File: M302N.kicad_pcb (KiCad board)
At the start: 2 copper layers, 100.1 x 56 mm, 31 parts, among them J1 DC12V, J10 ADC_IN, J11 RJ45, J12 DC12V FAN, J13 Conn_01x05_Socket, J14 Conn_01x05_Socket, J18 Conn_01x04_Socket, J19 Conn_01x04_Socket, J2 UART, J3 extend I/O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

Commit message: PCBほぼ完成
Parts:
- added REF**: MountingHole_2.7mm_M2.5_Pad, MountingHole:MountingHole_2.7mm_M2.5_Pad, F.Cu at (167.0, 109.9)
- added REF**: MountingHole_2.7mm_M2.5_Pad, MountingHole:MountingHole_2.7mm_M2.5_Pad, F.Cu at (81.3, 62.9)
- added REF**: MountingHole_2.7mm_M2.5_Pad, MountingHole:MountingHole_2.7mm_M2.5_Pad, F.Cu at (167.0, 62.9)
- added REF**: MountingHole_2.7mm_M2.5_Pad, MountingHole:MountingHole_2.7mm_M2.5_Pad, F.Cu at (75.6, 109.9)
- moved R1 5.20 mm to (80.6, 105.4), turned to 90 degrees
- moved C6 2.03 mm to (88.1, 64.8), turned to 0 degrees
- moved J19 0.27 mm to (132.8, 79.9)
- turned C4 to 90 degrees
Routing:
- net Net-(D2-K): track 8.78 -> 6.16 mm
- net +5V: track 160.8 -> 162.0 mm
- net /*D3: track 77.6 -> 76.8 mm
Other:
- board text added: "+"
- board text added: "+12V"
- board text added: "+5V"
- board text added: "A"
- board text added: "A0"
- board text added: "A1"
- board text added: "A2"
- board text added: "D4"
- board text added: "D5"
- board text added: "D6"
- board text added: "D7"
- board text added: "D8"
- board text added: "D9"
- board text added: "GND"
- board text added: "K"
- board text added: "M302N Ver. 1.00 2025 Mar."
- board text added: "RX"
- board text added: "SIG"
- board text added: "TX"
- board text added: "UECS観測ノード"
- board text added: "YS Lab"

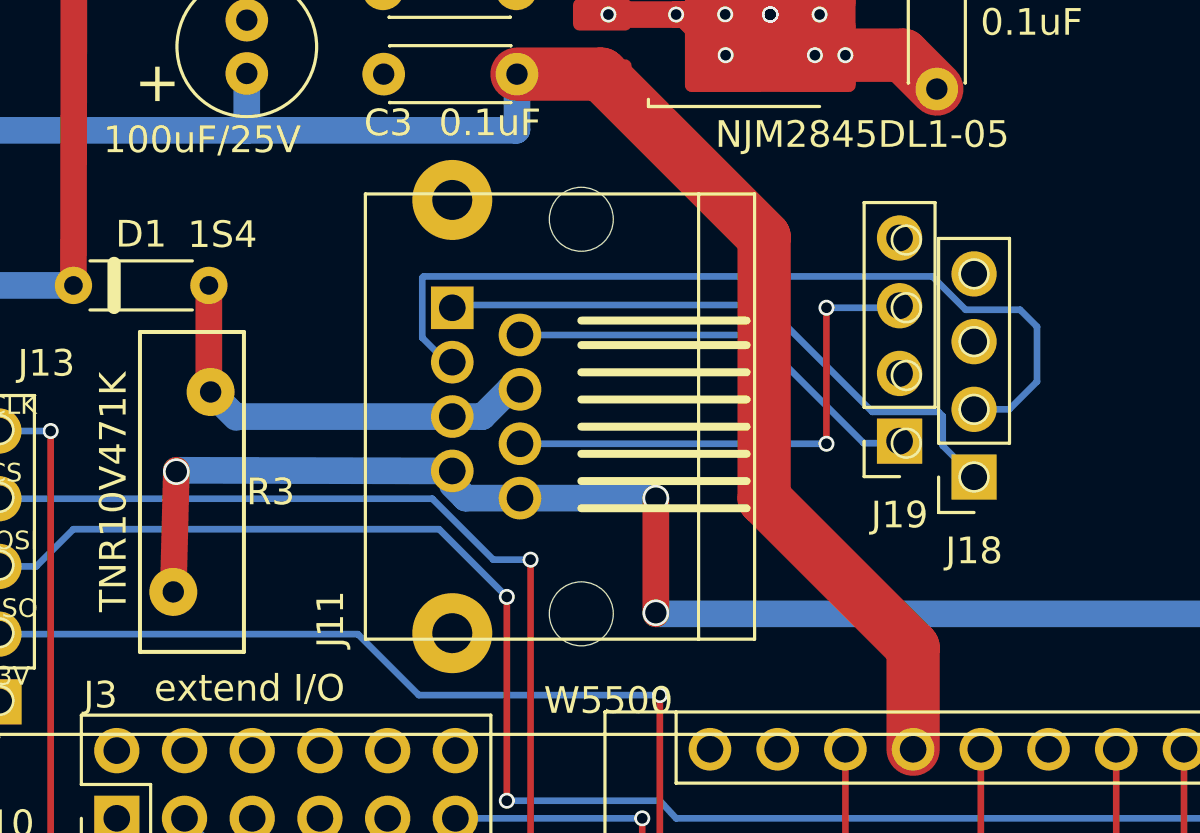
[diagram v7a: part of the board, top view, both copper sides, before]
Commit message: 3Dデータ更新とRJ45コネクタの取り付け位置微妙に変更
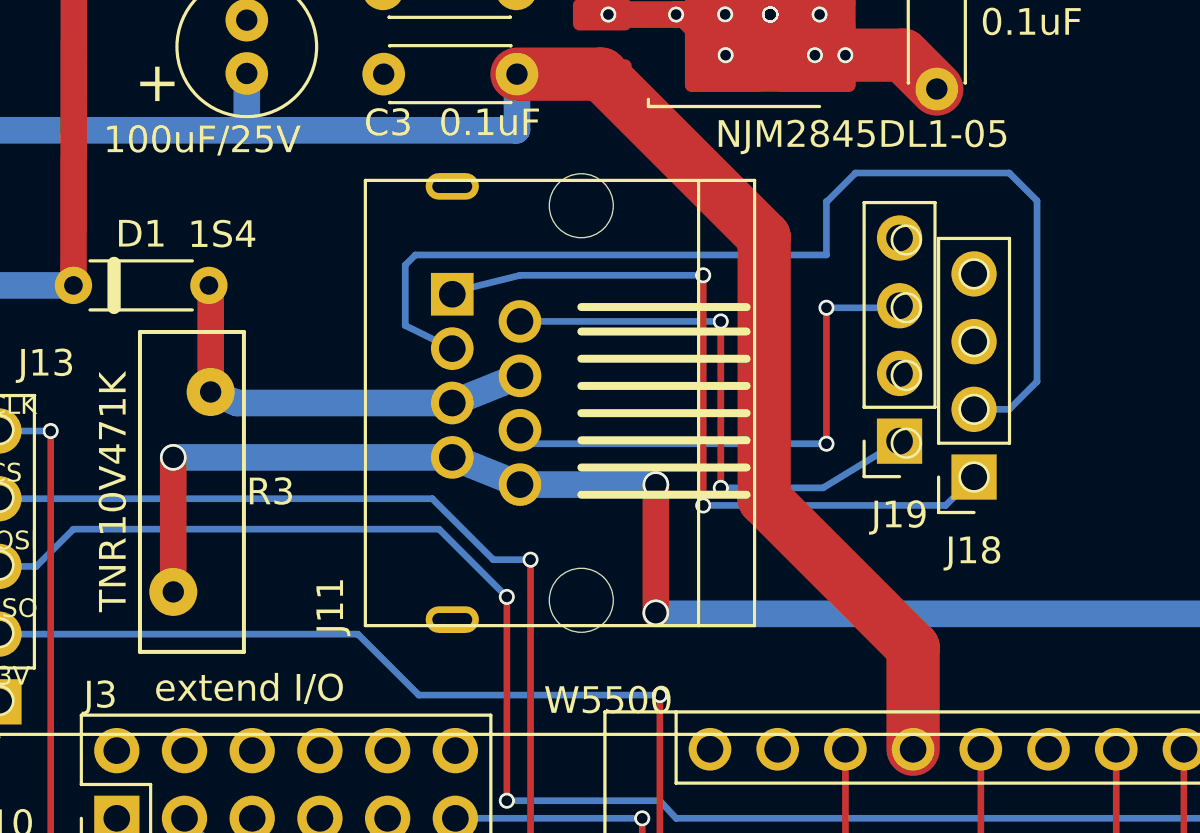
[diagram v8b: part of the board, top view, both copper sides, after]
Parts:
- moved J11 0.51 mm to (120.9, 78.5)
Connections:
- J11 pad : (no net) -> GND
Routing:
- net Net-(J18-Pin_2): track 32.5 -> 40.5 mm
- net Net-(J18-Pin_1): track 22.9 -> 28.8 mm, vias 0 -> 2
- net Net-(J19-Pin_1): track 16.2 -> 21.0 mm, vias 0 -> 2
- net Net-(J1-Pad2): track 75.5 -> 76.1 mm
- net Net-(D1-A): track 16.4 -> 15.9 mm
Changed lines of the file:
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@@
 	(footprint "HOLLY2:RJ45_Neltron_7810-8P8C"
 		(layer "F.Cu")
-		(at 120.904 78.96 90)
+		(at 120.904 78.452 90)
 		(descr "RJ45 Socket 秋月通商 http://akizukidenshi.com/catalog/g/gC-00159/")
 		(property "Reference" "J11"
@@
 			(layer "F.CrtYd")
 		)
-		(pad "" thru_hole circle
+		(pad "" thru_hole oval
 			(at -8.125 -4.84 90)
-			(size 3 3)
-			(drill 1.5)
+			(size 1 2)
+			(drill oval 0.5 1.5)
 			(layers "*.Cu" "*.Mask" "In1.Cu" "In2.Cu" "In3.Cu" "In4.Cu" "In5.Cu" "In6.Cu"
 				"In7.Cu" "In8.Cu" "In9.Cu" "In10.Cu" "In11.Cu" "In12.Cu" "In13.Cu" "In14.Cu"
@@
 			)
 			(remove_unused_layers no)
+			(net 13 "GND")
 		)
 		(pad "" np_thru_hole circle
@@
 			)
 		)
-		(pad "" thru_hole circle
+		(pad "" thru_hole oval
 			(at 8.125 -4.84 90)
-			(size 3 3)
-			(drill 1.5)
+			(size 1 2)
+			(drill oval 0.5 1.5)
 			(layers "*.Cu" "*.Mask" "In1.Cu" "In2.Cu" "In3.Cu" "In4.Cu" "In5.Cu" "In6.Cu"
 				"In7.Cu" "In8.Cu" "In9.Cu" "In10.Cu" "In11.Cu" "In12.Cu" "In13.Cu" "In14.Cu"
@@
 			)
 			(remove_unused_layers no)
+			(net 13 "GND")
 		)
 		(pad "1" thru_hole rect
@@
 		)
 		(pad "2" thru_hole circle
-			(at 7.5 1.4 90)
+			(at 7.5 1.401 90)
 			(size 1.8 1.8)
 			(drill 0.8)
@@
 		(tags "C Disc series Radial pin pitch 5.00mm  diameter 4.3mm width 1.9mm Capacitor")
 		(property "Reference" "C6"
-			(at 0.04 -2.159 360)
+			(at 0.04 -2.159 0)
 			(layer "F.SilkS")
 			(effects
@@
 	)
 	(segment
-		(start 106.934 74.041)
-		(end 106.934 77.973)
+		(start 107 74.041)
+		(end 107 77.973)
 		(width 1)
 		(layer "F.Cu")
@@
 	)
 	(segment
-		(start 116.064 78.96)
-		(end 117.19537 78.96)
-		(width 1)
-		(layer "B.Cu")
-		(net 25)
-	)
-	(segment
 		(start 106.934 77.973)
 		(end 106.999 78.038)
@@
 	)
 	(segment
-		(start 117.19537 78.96)
-		(end 118.21537 77.94)
+		(start 116.064 78.452)
+		(end 118.604 77.432)
 		(width 1)
 		(layer "B.Cu")
@@
 	(segment
 		(start 106.999 78.038)
-		(end 107.955 78.994)
-		(width 1)
-		(layer "B.Cu")
-		(net 25)
-	)
-	(segment
-		(start 107.989 78.96)
-		(end 116.064 78.96)
+		(end 107.989 78.452)
 		(width 1)
 		(layer "B.Cu")
@@
 	)
 	(segment
-		(start 118.21537 77.94)
-		(end 118.604 77.94)
+		(start 107.989 78.452)
+		(end 116.064 78.452)
 		(width 1)
 		(layer "B.Cu")
@@
 	)
 	(segment
-		(start 123.7 82.02)
+		(start 123.7 81.512)
 		(end 123.7 86.36)
 		(width 1)
@@
 	)
 	(segment
-		(start 105.7148 80.9752)
-		(end 105.713511 81.026)
-		(width 1)
-		(layer "F.Cu")
-		(net 27)
-	)
-	(segment
-		(start 105.713511 81.026)
+		(start 105.599 80.492)
 		(end 105.599 85.538)
 		(width 1)
@@
 	)
 	(via
-		(at 123.7 82.02)
+		(at 123.7 81.512)
 		(size 1)
 		(drill 0.8)
@@
 	)
 	(via
-		(at 105.713511 81.026)
+		(at 105.599 80.492)
 		(size 1)
 		(drill 0.8)
@@
 	)
 	(segment
-		(start 116.064 81)
-		(end 116.064 81.52)
-		(width 0.25)
-		(layer "B.Cu")
-		(net 27)
-	)
-	(segment
-		(start 116.064 81)
-		(end 105.7148 80.9752)
-		(width 1)
-		(layer "B.Cu")
-		(net 27)
-	)
-	(segment
-		(start 118.604 82.02)
-		(end 123.7 82.02)
+		(start 116.064 80.492)
+		(end 105.599 80.492)
 		(width 1)
 		(layer "B.Cu")
@@
 	)
 	(segment
-		(start 116.064 81.52)
-		(end 116.564 82.02)
+		(start 118.604 81.512)
+		(end 123.7 81.512)
 		(width 1)
 		(layer "B.Cu")
@@
 	)
 	(segment
-		(start 116.564 82.02)
-		(end 118.604 82.02)
+		(start 116.064 80.492)
+		(end 118.604 81.512)
 		(width 1)
 		(layer "B.Cu")
@@
 	)
 	(segment
-		(start 118.604 75.9)
-		(end 127.4366 75.9)
+		(start 126.136 75.392)
+		(end 126.136 81.636)
 		(width 0.25)
-		(layer "B.Cu")
+		(layer "F.Cu")
+		(net 28)
+	)
+	(via
+		(at 126.136 75.392)
+		(size 0.6)
+		(drill 0.4)
+		(layers "F.Cu" "B.Cu")
+		(net 28)
+	)
+	(via
+		(at 126.136 81.636)
+		(size 0.6)
+		(drill 0.4)
+		(layers "F.Cu" "B.Cu")
 		(net 28)
 	)
 	(segment
-		(start 127.4366 75.9)
-		(end 131.4958 79.9592)
+		(start 126.136 81.636)
+		(end 129.9718 81.636)
 		(width 0.25)
 		(layer "B.Cu")
@@
 	)
 	(segment
-		(start 131.4958 79.9592)
-		(end 133.096 79.9592)
+		(start 118.604 75.392)
+		(end 126.136 75.392)
 		(width 0.25)
 		(layer "B.Cu")
@@
 	)
 	(segment
-		(start 116.169 74.775)
-		(end 127.8102 74.775)
+		(start 129.9718 81.636)
+		(end 132.842 79.883)
 		(width 0.25)
 		(layer "B.Cu")
-		(net 29)
+		(net 28)
 	)
 	(segment
-		(start 127.8102 74.775)
-		(end 131.8194 78.7842)
+		(start 125.476 73.66)
+		(end 125.476 82.296)
 		(width 0.25)
-		(layer "B.Cu")
+		(layer "F.Cu")
+		(net 29)
+	)
+	(via
+		(at 125.476 73.66)
+		(size 0.6)
+		(drill 0.4)
+		(layers "F.Cu" "B.Cu")
+		(net 29)
+	)
+	(via
+		(at 125.476 82.296)
+		(size 0.6)
+		(drill 0.4)
+		(layers "F.Cu" "B.Cu")
 		(net 29)
 	)
 	(segment
-		(start 134.302 78.7842)
-		(end 134.461 78.9432)
+		(start 116.169 74.267)
+		(end 118.618 73.66)
 		(width 0.25)
 		(layer "B.Cu")
@@
 	)
 	(segment
-		(start 134.461 80.0542)
-		(end 135.636 81.2292)
+		(start 118.618 73.66)
+		(end 125.476 73.66)
 		(width 0.25)
 		(layer "B.Cu")
@@
 	)
 	(segment
-		(start 134.461 78.9432)
-		(end 134.461 80.0542)
+		(start 125.476 82.296)
+		(end 134.5692 82.296)
 		(width 0.25)
 		(layer "B.Cu")
@@
 	)
 	(segment
-		(start 131.8194 78.7842)
-		(end 134.302 78.7842)
+		(start 134.5692 82.296)
+		(end 135.636 81.2292)
 		(width 0.25)
 		(layer "B.Cu")
@@
 	)
 	(segment
-		(start 114.939 73.755)
-		(end 114.9898 73.7042)
+		(start 136.9568 78.6892)
+		(end 135.636 78.6892)
 		(width 0.25)
 		(layer "B.Cu")
@@
 	)
 	(segment
-		(start 136.9568 78.6892)
-		(end 135.636 78.6892)
+		(start 137.9982 70.866)
+		(end 137.9982 77.6478)
+		(width 0.25)
+		(layer "B.Cu")
+		(net 30)
+	)
+	(segment
+		(start 114.3 73.279)
+		(end 114.681 72.898)
 		(width 0.25)
 		(layer "B.Cu")
@@
 	)
 	(segment
-		(start 115.854 76.92)
-		(end 114.939 76.005)
+		(start 136.9568 69.8246)
+		(end 137.9982 70.866)
 		(width 0.25)
 		(layer "B.Cu")
@@
 	)
 	(segment
-		(start 134.069299 73.7042)
-		(end 135.320499 74.9554)
+		(start 114.681 72.898)
+		(end 130.1 72.898)
 		(width 0.25)
 		(layer "B.Cu")
@@
 	)
 	(segment
-		(start 137.3632 74.9554)
-		(end 137.9982 75.5904)
+		(start 114.3 75.547)
+		(end 114.3 73.279)
 		(width 0.25)
 		(layer "B.Cu")
@@
 	)
 	(segment
-		(start 114.9898 73.7042)
-		(end 134.069299 73.7042)
+		(start 131.191 69.8246)
+		(end 136.9568 69.8246)
 		(width 0.25)
 		(layer "B.Cu")
@@
 	)
 	(segment
-		(start 114.939 76.005)
-		(end 114.939 73.755)
+		(start 130.1 72.898)
+		(end 130.1 70.8902)
 		(width 0.25)
 		(layer "B.Cu")
@@
 	)
 	(segment
-		(start 137.9982 75.5904)
-		(end 137.9982 77.6478)
+		(start 116.064 76.412)
+		(end 114.3 75.547)
 		(width 0.25)
 		(layer "B.Cu")
@@
 	)
 	(segment
-		(start 116.064 76.92)
-		(end 115.854 76.92)
+		(start 130.1 70.8902)
+		(end 130.1254 70.8902)
 		(width 0.25)
 		(layer "B.Cu")
@@
 	)
 	(segment
-		(start 135.320499 74.9554)
-		(end 137.3632 74.9554)
+		(start 130.1254 70.8902)
+		(end 131.191 69.8246)
 		(width 0.25)
 		(layer "B.Cu")
